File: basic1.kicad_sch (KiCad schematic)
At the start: 3 parts

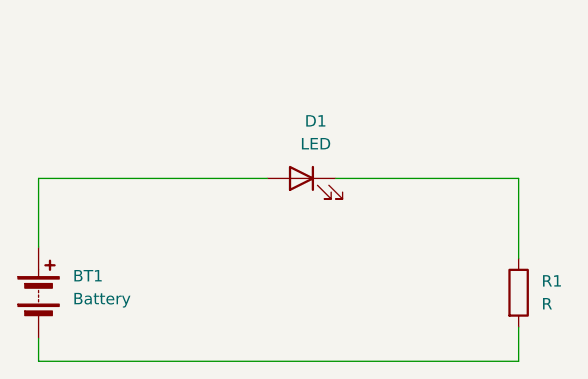
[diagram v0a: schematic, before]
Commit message: another led added
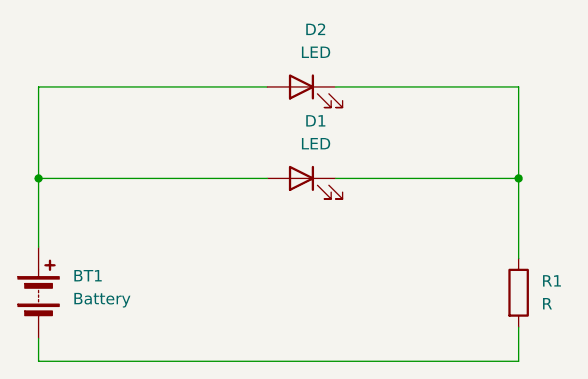
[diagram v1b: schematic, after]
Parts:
- added D2: LED, symbol Device:LED
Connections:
- net at BT1.1 (+), D1.2 (A): now also D2.2 (A)
- net at D1.1 (K), R1.1: now also D2.1 (K)
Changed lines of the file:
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@@
 	(generator_version "9.0")
 	(paper "A4")
+	(junction
+		(at 180.34 72.39)
+		(diameter 0)
+		(color 0 0 0 0)
+	)
+	(junction
+		(at 127 72.39)
+		(diameter 0)
+		(color 0 0 0 0)
+	)
+	(wire
+		(pts
+			(xy 160.02 62.23) (xy 180.34 62.23)
+		)
+		(stroke
+			(width 0)
+			(type default)
+		)
+	)
 	(wire
 		(pts
@@
 	(wire
 		(pts
+			(xy 127 62.23) (xy 127 72.39)
+		)
+		(stroke
+			(width 0)
+			(type default)
+		)
+	)
+	(wire
+		(pts
+			(xy 180.34 62.23) (xy 180.34 72.39)
+		)
+		(stroke
+			(width 0)
+			(type default)
+		)
+	)
+	(wire
+		(pts
 			(xy 180.34 72.39) (xy 180.34 81.28)
+		)
+		(stroke
+			(width 0)
+			(type default)
+		)
+	)
+	(wire
+		(pts
+			(xy 152.4 62.23) (xy 127 62.23)
 		)
 		(stroke
@@
 					(unit 1)
 				)
+			)
+		)
+	)
+	(symbol
+		(lib_id "Device:LED")
+		(at 156.21 62.23 0)
+		(mirror y)
+		(unit 1)
+		(exclude_from_sim no)
+		(in_bom yes)
+		(on_board yes)
+		(dnp no)
+		(property "Reference" "D2"
+			(at 157.7975 55.88 0)
+			(effects
+				(font
+					(size 1.27 1.27)
+				)
+			)
+		)
+		(property "Value" "LED"
+			(at 157.7975 58.42 0)
+			(effects
+				(font
+					(size 1.27 1.27)
+				)
+			)
+		)
+		(property "Footprint" ""
+			(at 156.21 62.23 0)
+			(effects
+				(font
+					(size 1.27 1.27)
+				)
+				(hide yes)
+			)
+		)
+		(property "Datasheet" "~"
+			(at 156.21 62.23 0)
+			(effects
+				(font
+					(size 1.27 1.27)
+				)
+				(hide yes)
+			)
+		)
+		(property "Description" "Light emitting diode"
+			(at 156.21 62.23 0)
+			(effects
+				(font
+					(size 1.27 1.27)
+				)
+				(hide yes)
+			)
+		)
+		(property "Sim.Pins" "1=K 2=A"
+			(at 156.21 62.23 0)
+			(effects
+				(font
+					(size 1.27 1.27)
+				)
+				(hide yes)
+			)
+		)
+		(pin "1"
+		)
+		(pin "2"
+		)
+		(instances
+			(project "basic1"
+				(path "/ae09a829-f66c-42b3-baaa-271b279764a4"
+					(reference "D2")
+					(unit 1)
+				)
